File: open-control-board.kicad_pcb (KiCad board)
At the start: 4 copper layers, 69 x 54 mm, 123 parts, among them CN1 Service boiler fill sensor, CN10 LCC Port, CN2 Water tank level switch, CN3 NTC Service Boiler, CN4 NTC Brew Boiler, CN5 Service boiler relay, CN6 Conn_02x04_Counter_Clockwise, CN7 Brew Switch, CN8 12V Separate Supply, CN9 Brew boiler relay, J1 USB_B_Micro, J10 Conn_01x04_Pin, J11 Conn_01x04_Pin, J12 Conn_02x06_Odd_Even, J13 Conn_02x05_Odd_Even, J14 Conn_02x04_Odd_Even, J15 Conn_02x05_Odd_Even, J16 USB_B_Micro, J17 BM04B-SRSS-TB(LF)(SN), J18 Conn_01x03_Pin, J2 BM04B-SRSS-TB(LF)(SN), Q1 AO3401A, Q11 DMN63D8LDW, Q2 AO3401A, Q3 Q_PMOS-E_DUAL_Generic_SEP_S1G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, Q4 DMN63D8LDW, Q5 Q_PMOS-E_DUAL_Generic_SEP_S1G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, Q6 DMN63D8LDW, SW1 SW_Push, SW2 SW_Push, SW3 SW_Push, SW4 SW_Push, U1 TPS82130, U10 FDC1004, U15 STPIC6C595TTR, U16 STPIC6C595TTR, U3 TPS82130, U4 RP2040, U5 ESP32-S3-WROOM-1, U7 TXB0108PWR, U8 ADS1115IDGS, U9 W25Q16JVUXIQ, Y1 XYDBPCNANF-12MHZ

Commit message: Added OSHW logo
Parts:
- added REF**: OSHW-Logo2_9.8x8mm_SilkScreen, Symbol:OSHW-Logo2_9.8x8mm_SilkScreen, B.Cu at (108.0, 59.6)
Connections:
- Q4 pad 3: unconnected-(Q4B-D2-Pad3) -> (no net)
- Q4 pad 4: unconnected-(Q4B-S2-Pad4) -> (no net)
- Q4 pad 5: unconnected-(Q4B-G2-Pad5) -> (no net)

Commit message: R0B changes (WIP)
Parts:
- removed CN1: Service boiler fill sensor, Connector_PinHeader_2.54mm:PinHeader_1x02_P2.54mm_Vertical
- removed D3: KT-0603W, LED_SMD:LED_0603_1608Metric
- removed J10, J11: Conn_01x04_Pin, Connector_PinSocket_2.54mm:PinSocket_1x04_P2.54mm_Vertical
- removed J14: Conn_02x04_Odd_Even, Connector_PinHeader_2.54mm:PinHeader_2x04_P2.54mm_Vertical
- removed J18: Conn_01x03_Pin, Connector_PinHeader_2.54mm:PinHeader_1x03_P2.54mm_Vertical_SMD_Pin1Left
- removed R35: 120R, Resistor_SMD:R_0402_1005Metric
- removed R49, R50: 10K, Resistor_SMD:R_0402_1005Metric
- added C26: C_Small, Capacitor_SMD:C_0402_1005Metric_Pad0.74x0.62mm_HandSolder, F.Cu at (103.4, 33.4)
- added C35: C_Small, Capacitor_SMD:C_0402_1005Metric_Pad0.74x0.62mm_HandSolder, F.Cu at (104.5, 34.5)
- added C36: C_Small, Capacitor_SMD:C_0402_1005Metric_Pad0.74x0.62mm_HandSolder, F.Cu at (108.8, 34.8)
- added C38: C_Small, Capacitor_SMD:C_0402_1005Metric_Pad0.74x0.62mm_HandSolder, F.Cu at (109.8, 33.5)
- added C39: C_Small, Capacitor_SMD:C_0402_1005Metric_Pad0.74x0.62mm_HandSolder, F.Cu at (112.8, 35.8)
- added C40: C_Small, Capacitor_SMD:C_0402_1005Metric_Pad0.74x0.62mm_HandSolder, F.Cu at (112.8, 37.0)
- added C41: C_Small, Capacitor_SMD:C_0402_1005Metric_Pad0.74x0.62mm_HandSolder, F.Cu at (112.8, 42.4)
- added C42: C_Small, Capacitor_SMD:C_0402_1005Metric_Pad0.74x0.62mm_HandSolder, F.Cu at (112.8, 43.6)
- added C43: C_Small, Capacitor_SMD:C_0805_2012Metric_Pad1.18x1.45mm_HandSolder, F.Cu at (110.6, 36.8)
- added C44: C_Small, Capacitor_SMD:C_0805_2012Metric_Pad1.18x1.45mm_HandSolder, F.Cu at (110.6, 43.0)
- added D2: KT-0603W, LED_SMD:LED_0603_1608Metric, F.Cu at (71.9, 46.0)
- added J3: Conn_02x03_Odd_Even, Connector_PinHeader_1.27mm:PinHeader_2x03_P1.27mm_Vertical_SMD, B.Cu at (76.3, 58.1)
- added J4: Conn_01x06_Pin, Connector_PinHeader_2.54mm:PinHeader_1x06_P2.54mm_Vertical, F.Cu at (119.2, 32.9)
- added J5: Conn_02x05_Counter_Clockwise, Connector_PinHeader_2.54mm:PinHeader_2x05_P2.54mm_Vertical, F.Cu at (76.9, 29.9)
- added J6: Conn_01x05_Pin, Connector_PinHeader_2.54mm:PinHeader_1x05_P2.54mm_Vertical, F.Cu at (54.4, 41.8)
- added JP1: SolderJumper_3_Bridged12, Jumper:SolderJumper-3_P1.3mm_Bridged2Bar12_RoundedPad1.0x1.5mm_NumberLabels, B.Cu at (110.7, 52.9)
- added JP10: SolderJumper_3_Bridged12, Jumper:SolderJumper-3_P1.3mm_Bridged2Bar12_RoundedPad1.0x1.5mm_NumberLabels, B.Cu at (110.7, 55.6)
- added JP11: SolderJumper_3_Bridged12, Jumper:SolderJumper-3_P1.3mm_Bridged2Bar12_RoundedPad1.0x1.5mm_NumberLabels, B.Cu at (110.7, 58.2)
- added JP12: SolderJumper_3_Bridged12, Jumper:SolderJumper-3_P1.3mm_Bridged2Bar12_RoundedPad1.0x1.5mm_NumberLabels, B.Cu at (110.7, 60.9)
- added JP14: SolderJumper_2_Open, Jumper:SolderJumper-2_P1.3mm_Open_RoundedPad1.0x1.5mm, B.Cu at (111.2, 41.1)
- added JP15: SolderJumper_2_Open, Jumper:SolderJumper-2_P1.3mm_Open_RoundedPad1.0x1.5mm, B.Cu at (111.2, 46.2)
- added JP16: SolderJumper_3_Bridged12, Jumper:SolderJumper-3_P1.3mm_Bridged2Bar12_RoundedPad1.0x1.5mm_NumberLabels, B.Cu at (60.5, 53.5)
- added JP17: SolderJumper_2_Bridged, Jumper:SolderJumper-2_P1.3mm_Bridged2Bar_RoundedPad1.0x1.5mm, F.Cu at (115.2, 30.9)
- added JP18: SolderJumper_2_Bridged, Jumper:SolderJumper-2_P1.3mm_Bridged2Bar_RoundedPad1.0x1.5mm, F.Cu at (105.7, 30.8)
- added Q7: DMN63D8LDW, PCM_Package_TO_SOT_SMD_AKL:SOT-363_SC-70-6, F.Cu at (93.2, 46.8)
- added R14: R_Small, Resistor_SMD:R_0805_2012Metric_Pad1.20x1.40mm_HandSolder, F.Cu at (98.8, 33.2)
- added R15: R_Small, Resistor_SMD:R_0805_2012Metric_Pad1.20x1.40mm_HandSolder, F.Cu at (106.5, 37.0)
- added R16: R_Small, Resistor_SMD:R_0402_1005Metric_Pad0.72x0.64mm_HandSolder, F.Cu at (107.6, 33.5)
- added R25: R_Small, Resistor_SMD:R_0402_1005Metric_Pad0.72x0.64mm_HandSolder, F.Cu at (115.2, 37.0)
- added R3: 10K, Resistor_SMD:R_0402_1005Metric, F.Cu at (106.0, 57.6)
- added R4: R_Small, Resistor_SMD:R_0402_1005Metric_Pad0.72x0.64mm_HandSolder, F.Cu at (102.2, 33.4)
- added R40: R_Small, Resistor_SMD:R_0805_2012Metric_Pad1.20x1.40mm_HandSolder, F.Cu at (115.2, 34.2)
- added R41: R_Small, Resistor_SMD:R_0805_2012Metric_Pad1.20x1.40mm_HandSolder, F.Cu at (115.2, 38.6)
- added R42: R_Small, Resistor_SMD:R_0805_2012Metric_Pad1.20x1.40mm_HandSolder, F.Cu at (115.2, 40.8)
- added R43: R_Small, Resistor_SMD:R_0805_2012Metric_Pad1.20x1.40mm_HandSolder, F.Cu at (115.2, 45.2)
- added RN3: 10K, PCM_Resistor_SMD_AKL:R_Array_Concave_4x0402, F.Cu at (107.6, 46.2)
- added U11: ADS1115IDGS, Package_SO:TSSOP-10_3x3mm_P0.5mm, F.Cu at (102.6, 41.5)
- added U12: ADS1115IDGS, Package_SO:TSSOP-10_3x3mm_P0.5mm, F.Cu at (102.6, 45.4)
- CN2: value Water tank level switch -> ~
- CN5: value Service boiler relay -> ~
- CN7: value Brew Switch -> ~
- CN9: value Brew boiler relay -> ~
- J1, J16: footprint U-D-M5DS-W-3:U-D-M5DS-W-3 -> Connector_USB:USB_Micro-B_Molex-105133-0001
- JP3, JP7: footprint Connector_PinHeader_2.54mm:PinHeader_1x02_P2.54mm_Vertical -> Connector_PinHeader_1.27mm:PinHeader_1x02_P1.27mm_Vertical
- R19: value R_Small -> 10K; footprint Resistor_THT:R_Axial_DIN0204_L3.6mm_D1.6mm_P5.08mm_Horizontal -> Resistor_SMD:R_0402_1005Metric
- R24, R26, R27: footprint Resistor_THT:R_Axial_DIN0204_L3.6mm_D1.6mm_P5.08mm_Horizontal -> Resistor_SMD:R_0402_1005Metric_Pad0.72x0.64mm_HandSolder
- R31: value 10K -> 120R
- U8: value ADS1115IDGS -> TXB0108PWR; footprint Package_SO:TSSOP-10_3x3mm_P0.5mm -> Package_SO:TSSOP-20_4.4x6.5mm_P0.65mm
- moved Q5 54.8 mm to (59.2, 43.4), turned to 180 degrees
- moved Q3 54.7 mm to (59.3, 47.6), turned to 180 degrees
- moved JP6 49.6 mm to (60.5, 50.1)
- moved JP4 49.6 mm to (60.4, 42.5)
- moved JP5 49.6 mm to (60.4, 46.2)
- moved R30 49.3 mm to (62.1, 46.6), turned to 90 degrees
- moved R29 49.2 mm to (62.1, 44.5), turned to 90 degrees
- moved R28 49.1 mm to (62.1, 42.4), turned to 90 degrees
- moved R19 48.6 mm to (62.1, 48.6), turned to 90 degrees
- moved J17 35.7 mm to (65.5, 53.5)
- moved R36 35.7 mm to (64.0, 55.3)
- moved R37 35.7 mm to (66.0, 55.3)
- moved J15 28.6 mm to (87.4, 58.0)
- moved R20 27.0 mm to (97.3, 58.9), turned to 0 degrees
- moved R21 26.3 mm to (97.3, 57.8), turned to 0 degrees
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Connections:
- net GP15 renamed RP2040_SERIAL_BOOT
- C2 pad 2: +12V -> VIN
- CN2 pad 1: WATER_TANK_LVL_SW -> VIN
- CN2 pad 2: GND -> CN9_DRAIN
- CN3 pad 1: AVCC -> ADC1_AIN2_COND
- CN3 pad 2: SERVICE_BOILER_NTC -> ADC1_AIN3
- CN4 pad 1: AVCC -> ADC1_AIN0_COND
- CN4 pad 2: BREW_BOILER_NTC -> ADC1_AIN1
- CN5 pad 1: CN5_DRAIN -> VIN
- CN5 pad 2: +12V -> CN5_DRAIN
- CN6 pad 2: +12V -> VIN
- CN7 pad 1: BREW_SW -> WATER_TANK_LVL_SW
- CN8 pad 1: +12V -> VIN
- CN9 pad 1: +12V -> BREW_SW
- CN9 pad 2: CN9_DRAIN -> GND
- J12 pad 2: +3V3 -> +5V
- JP2 pad 1: +12V -> VIN
- JP3 pad 2: +5V -> VIN
- JP4 pad 1: +12V -> VIN
- JP5 pad 1: +12V -> VIN
- JP6 pad 1: +12V -> VIN
- JP7 pad 2: +5V -> VIN
- Q2 pad 2: +12V -> VIN
- Q3 pad 1: VOUT_2_GATE -> VOUT_4_GATE
- Q3 pad 5: Net-(JP5-C) -> Net-(JP16-C)
- Q3 pad 6: VOUT_2 -> VOUT_4
- Q4 pad 1: ADS1115_RDY -> INT_SCL
- Q4 pad 3: (no net) -> INT_SDA_AVCC
- Q4 pad 4: (no net) -> INT_SDA
- Q4 pad 5: (no net) -> +3V3
- Q4 pad 6: ADS1115_RDY_AVCC -> INT_SCL_AVCC
- Q5 pad 1: (no net) -> VOUT_2_GATE
- Q5 pad 5: (no net) -> Net-(JP5-C)
- Q5 pad 6: (no net) -> VOUT_2
- Q6 pad 1: INT_SDA -> ADS1115_1_RDY
- Q6 pad 3: INT_SCL_AVCC -> ADS1115_2_RDY_AVCC
- Q6 pad 4: INT_SCL -> ADS1115_2_RDY
- Q6 pad 6: INT_SDA_AVCC -> ADS1115_1_RDY_AVCC
- R19 pad 1: AGND -> Net-(JP16-C)
- R19 pad 2: AIN1 -> VOUT_4_GATE
- R2 pad 2: +12V -> VIN
- R20 pad 1: INT_SDA -> INT_SCL
- R21 pad 1: INT_SCL -> INT_SDA
- R24 pad 1: AGND -> ADC2_AIN0_COND
- R24 pad 2: AIN0 -> ADC2_AIN0
- R26 pad 1: SERVICE_BOILER_NTC -> ADC2_AIN2_COND
- R26 pad 2: AGND -> ADC2_AIN2
- R27 pad 1: AGND -> ADC2_AIN3_COND
- R27 pad 2: BREW_BOILER_NTC -> ADC2_AIN3
- R31 pad 1: SR_OE -> Net-(U5-GPIO8/TOUCH8/ADC1_CH7/SUBSPICS1)
- R31 pad 2: GND -> Net-(D2-A)
- RN2 pad 1: INT_SDA_AVCC -> INT_SCL
- RN2 pad 2: INT_SCL_AVCC -> INT_SDA
- RN2 pad 3: INT_SDA -> INT_SDA_AVCC
- RN2 pad 4: INT_SCL -> INT_SCL_AVCC
- RN2 pad 5: +3V3 -> AVCC
- RN2 pad 6: +3V3 -> AVCC
- RN2 pad 7: AVCC -> +3V3
- RN2 pad 8: AVCC -> +3V3
- U1 pad 1: +12V -> VIN
- U1 pad 2: +12V -> VIN
- U16 pad 12: unconnected-(U16-DRAIN5-Pad12) -> VOUT_4_GATE
- U4 pad 11: INT_SCL -> INT_SDA
- U4 pad 12: INT_SDA -> INT_SCL
- U4 pad 13: ESP32_RP2040_UART1 -> SRCK_3V3
- U4 pad 14: ESP32_RP2040_UART2 -> unconnected-(U4-GPIO11-Pad14)
- U4 pad 29: GP18 -> GP18_3V3
- U4 pad 30: GP19 -> GP19_3V3
- U4 pad 31: GP20 -> GP20_3V3
- U4 pad 32: GP21 -> GP21_3V3
- U4 pad 6: SRCK_3V3 -> ESP32_RP2040_UART1
- U4 pad 7: ADS1115_RDY -> ESP32_RP2040_UART2
- U4 pad 8: QWIIC_SCL -> QWIIC_SDA
- U4 pad 9: QWIIC_SDA -> QWIIC_SCL
- U5 pad 11: ESP32_RP2040_UART1 -> unconnected-(U5-GPIO18/U1RXD/ADC2_CH7/CLK_OUT3-Pad11)
- U5 pad 12: GP26 -> Net-(U5-GPIO8/TOUCH8/ADC1_CH7/SUBSPICS1)
- U5 pad 17: GP27 -> unconnected-(U5-GPIO9/TOUCH9/ADC1_CH8/FSPIHD/SUBSPIHD-Pad17)
- U5 pad 18: GP28 -> ESP32_QWIIC_SDA
- U5 pad 19: GP29 -> ESP32_QWIIC_SCL
- U5 pad 23: ESP32_RP2040_UART2 -> unconnected-(U5-GPIO21-Pad23)
- U5 pad 25: Net-(U5-GPIO48/SPICLK_N/SUBSPICLK_N_DIFF) -> unconnected-(U5-GPIO48/SPICLK_N/SUBSPICLK_N_DIFF-Pad25)
- U5 pad 36: Net-(J18-Pin_1) -> ESP32_U0RXD
- U5 pad 37: Net-(J18-Pin_2) -> ESP32_U0TXD
- U5 pad 38: ESP32_QWIIC_SDA -> ESP32_RP2040_UART2
- U5 pad 39: ESP32_QWIIC_SCL -> ESP32_RP2040_UART1
- U5 pad 4: GP18 -> GP18_3V3
- U5 pad 5: GP19 -> GP19_3V3
- U5 pad 6: GP20 -> GP20_3V3
- U5 pad 7: GP21 -> GP21_3V3
- U5 pad 8: unconnected-(U5-GPIO15/U0RTS/ADC2_CH4/XTAL_32K_P-Pad8) -> ESP32_BOOTSEL_RP2040
- U5 pad 9: unconnected-(U5-GPIO16/U0CTS/ADC2_CH5/XTAL_32K_N-Pad9) -> ESP32_DISABLE_RP2040
- U7 pad 1: CN6_2_3V3 -> CN6_4_3V3
- U7 pad 10: SER_IN_3V3 -> SR_OE
- U7 pad 11: SER_IN_5V -> GND
- U7 pad 12: SRCLR_5V -> SER_IN_5V
- U7 pad 13: nG_5V -> SRCLR_5V
- U7 pad 14: RCLK_5V -> nG_5V
- U7 pad 15: GND -> RCLK_5V
- U7 pad 16: +5V -> SRCK_5V
- U7 pad 17: SRCK_5V -> CN6_2_5V
- U7 pad 18: CN6_2_5V -> CN6_3_5V
- U7 pad 19: CN6_3_5V -> +5V
- U7 pad 2: CN6_3_3V3 -> +3V3
- U7 pad 3: CN6_4_3V3 -> CN6_3_3V3
- U7 pad 4: SRCK_3V3 -> CN6_2_3V3
- U7 pad 5: +3V3 -> SRCK_3V3
- U7 pad 6: SR_OE -> RCLK_3V3
- U7 pad 7: RCLK_3V3 -> nG_3V3
- U7 pad 8: nG_3V3 -> SRCLR_3V3
- U7 pad 9: SRCLR_3V3 -> SER_IN_3V3
- U8 pad 1: AGND -> GP21_3V3
- U8 pad 10: INT_SCL_AVCC -> SR_OE
- U8 pad 2: ADS1115_RDY_AVCC -> +3V3
- U8 pad 3: AGND -> GP20_3V3
- U8 pad 4: AIN0 -> GP19_3V3
- U8 pad 5: AIN1 -> GP18_3V3
- U8 pad 6: BREW_BOILER_NTC -> unconnected-(U8-A5-Pad6)
- U8 pad 7: SERVICE_BOILER_NTC -> unconnected-(U8-A6-Pad7)
- U8 pad 8: AVCC -> unconnected-(U8-A7-Pad8)
- U8 pad 9: INT_SDA_AVCC -> unconnected-(U8-A8-Pad9)
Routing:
- net +12V: track 233.6 -> 0.00 mm, vias 2 -> 0
- net VIN: track 0.00 -> 210.2 mm, vias 0 -> 2
- net GP21_3V3: track 0.00 -> 73.4 mm, vias 0 -> 3
- net GP19_3V3: track 0.00 -> 72.2 mm, vias 0 -> 3
- net GP18_3V3: track 0.00 -> 68.8 mm, vias 0 -> 3
- net GP20_3V3: track 0.00 -> 68.1 mm, vias 0 -> 3
- net ESP32_TMS: track 71.6 -> 13.7 mm, vias 1 -> 2
- net ESP32_TDO: track 63.7 -> 11.4 mm, vias 1 -> 2
- net ESP32_TDI: track 62.1 -> 9.99 mm, vias 1 -> 2
- net ESP32_TCK: track 65.1 -> 13.2 mm, vias 1 -> 2
- net +3V3: track 359.0 -> 311.8 mm, vias 18 -> 24
- net VOUT_4_GATE: track 0.00 -> 42.0 mm, vias 0 -> 2
- net GP19: track 50.8 -> 9.56 mm, vias 2 -> 0
- net GP20: track 50.5 -> 9.53 mm, vias 3 -> 0
- net Net-(J18-Pin_1): track 39.8 -> 0.00 mm, vias 2 -> 0
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- added copper zone on F.Cu, net VIN
- removed copper zone on F.Cu, net +12V
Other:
- board text added: "CN10 UART TX Verified"
- board text added: "J12 Verified"
- board text removed: "ESP32 EN"
- board text removed: "ESP32 GPIO0"
- board text removed: "RP2040 Boot"
- board text removed: "RP2040 Reset"

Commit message: WIP
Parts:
- removed C35, C36: C_Small, Capacitor_SMD:C_0402_1005Metric_Pad0.74x0.62mm_HandSolder
- C26, C38, C39, C40, C41, C42, C43, C44: value C_Small -> 100 nF
- R16, R24, R25, R26, R27, R4: value R_Small -> 1K
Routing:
- net AGND: track 20.8 -> 14.2 mm, vias 6 -> 7
- net ADC1_AIN0: track 11.2 -> 10.2 mm
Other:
- board text added: "Rev R0B"
- board text removed: "Rev R0A"

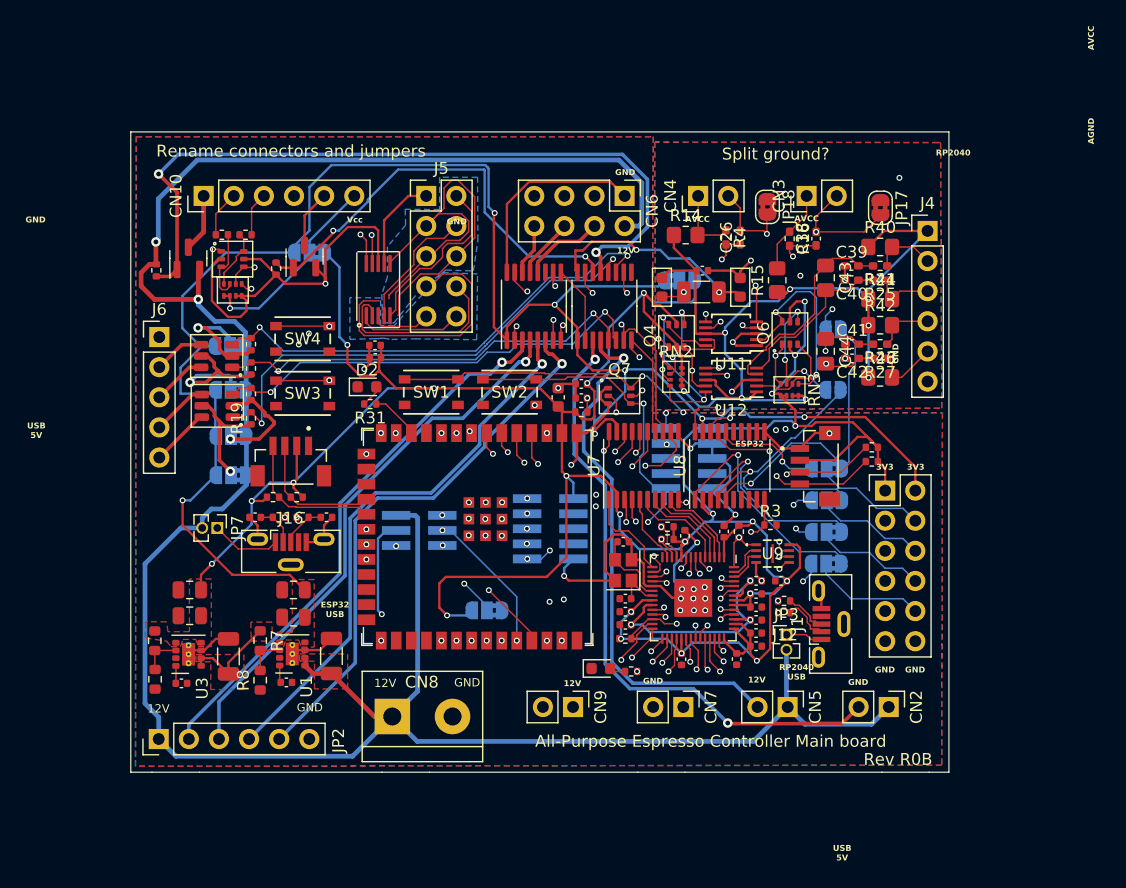
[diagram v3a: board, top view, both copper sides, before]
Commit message: Renamed connectors and added a lot of silk screen
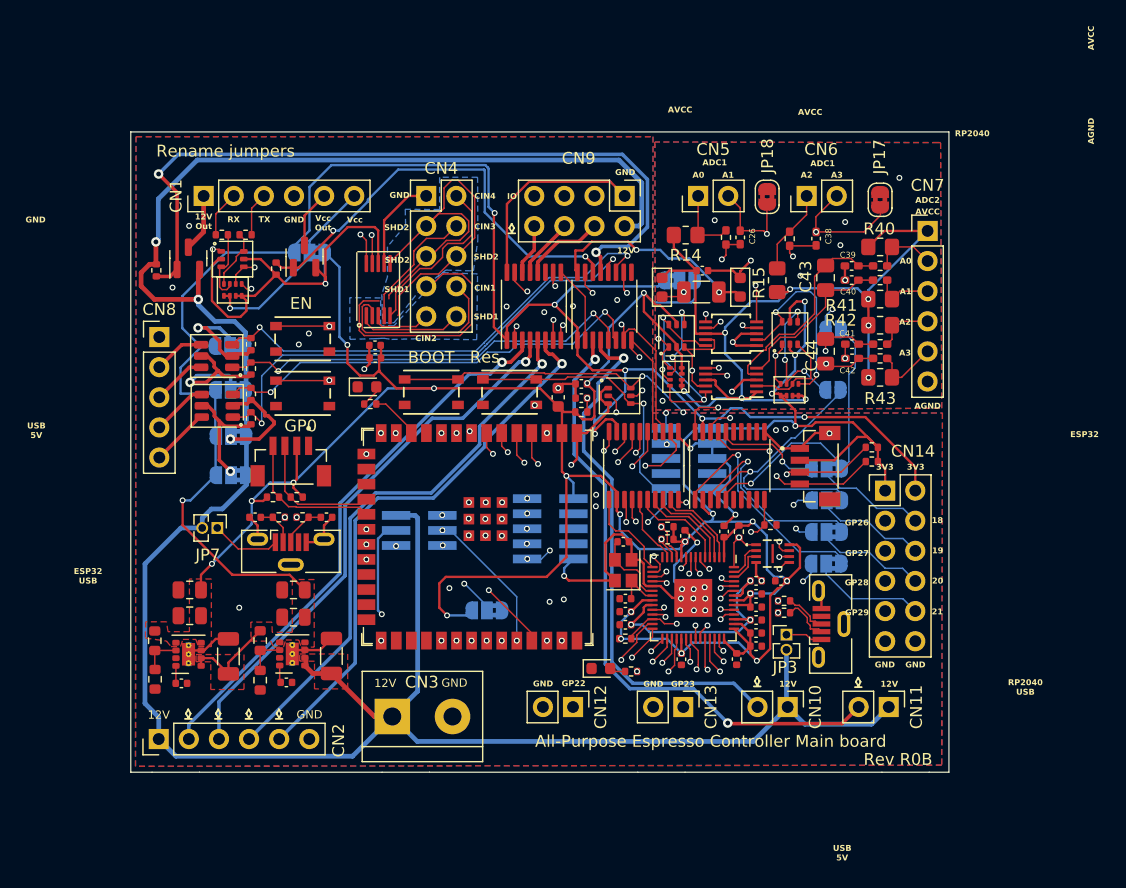
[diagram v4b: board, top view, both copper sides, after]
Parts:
- U7, U8: value TXB0108PWR -> TXS0108EPWR
- moved REF** 69.5 mm to (60.5, 67.8)
- moved JP18 0.85 mm to (105.7, 30.0)
- moved JP17 0.68 mm to (115.2, 30.2)
- renumbered CN10 to CN1, CN5 to CN10, CN2 to CN11, CN9 to CN12, CN7 to CN13, J12 to CN14, JP2 to CN2, CN8 to CN3, J5 to CN4, CN4 to CN5, CN3 to CN6, J4 to CN7, J6 to CN8, CN6 to CN9
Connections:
- net CN10_12V_GATE renamed CN1_12V_GATE
- net CN10_3V3_GATE renamed CN1_3V3_GATE
- net CN10_UART_RX renamed CN1_UART_RX
- net CN10_UART_RX_SHIFT_SEL renamed CN1_UART_RX_SHIFT_SEL
- net CN10_UART_TX renamed CN1_UART_TX
- net CN10_UART_TX_SHIFT_SEL renamed CN1_UART_TX_SHIFT_SEL
- net CN10_UART_VCC renamed CN1_UART_VCC
- net CN5_DRAIN renamed CN10_DRAIN
- net CN6_2_3V3 renamed CN9_2_3V3
- net CN6_2_5V renamed CN9_2_5V
- net CN6_3_3V3 renamed CN9_3_3V3
- net CN6_3_5V renamed CN9_3_5V
- net CN6_4 renamed CN9_4
- net CN6_4_3V3 renamed CN9_4_3V3
- net CN6_4_5V renamed CN9_4_5V
- net CN6_6 renamed CN9_6
- net CN6_8 renamed CN9_8
- net CN9_DRAIN renamed CN11_DRAIN
- net JP2_FA10 renamed CN2_FA10
- net JP2_FA7 renamed CN2_FA7
- net JP2_FA8 renamed CN2_FA8
- net JP2_FA9 renamed CN2_FA9
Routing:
- net ADC1_AIN1: track 14.9 -> 16.0 mm
- net ADC1_AIN3: track 23.0 -> 23.7 mm
- net GND: vias 31 -> 39
- net AGND: vias 7 -> 11
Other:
- board text added: "1"
- board text added: "12V Out"
- board text added: "18"
- board text added: "19"
- board text added: "2"
- board text added: "20"
- board text added: "21"
- board text added: "3"
- board text added: "4"
- board text added: "A0"
- board text added: "A1"
- board text added: "A2"
- board text added: "A3"
- board text added: "ADC1"
- board text added: "ADC1 RDY -> GP18"
- board text added: "ADC2"
- board text added: "ADC2 RDY -> GP19"
- board text added: "BOOT"
- board text added: "CIN1"
- board text added: "CIN2"
- board text added: "CIN3"
- board text added: "CIN4"
- board text added: "EN"
- board text added: "ESP-Prog JTAG"
- board text added: "ESP-Prog UART"
- board text added: "GP0"
- board text added: "GP18"
- board text added: "GP18-21 V"
- board text added: "GP19"
- board text added: "GP20"
- board text added: "GP21"
- board text added: "GP22"
- board text added: "GP23"
- board text added: "GP26"
- board text added: "GP27"
- board text added: "GP28"
- board text added: "GP29"
- board text added: "IO"
- board text added: "RESET"
- board text added: "RP2040 SWD"
- board text added: "Rename jumpers"
- board text added: "Res"
- board text added: "SHD1"
- board text added: "SHD2"
- board text added: "SWCLK"
- board text added: "SWD"
- board text added: "TCK"
- board text added: "TDI"
- board text added: "TDO"
- board text added: "TMS"
- board text added: "VIN"
- board text added: "VOUT V"
- board text added: "Vcc Out"
- board text removed: "RP2040 DBG"
- board text removed: "Rename connectors and jumpers"
- board text removed: "Split ground?"
- board text removed: "UART"
- board text removed: "VOUT1 V"
- board text removed: "VOUT2 V"
- board text removed: "VOUT3 V"

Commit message: Updated PCB with screw holes
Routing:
- net VIN: track 210.2 -> 209.1 mm
- net GND: vias 39 -> 41
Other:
- outline, holes or cut-outs redrawn
- board text removed: "ESP32"
- board text removed: "ESP32 JTAG"
- board text removed: "ESP32 USB"
- board text removed: "J12 Verified"
- board text removed: "RP2040"
- board text removed: "RP2040 USB"
- board text removed: "USB 5V"

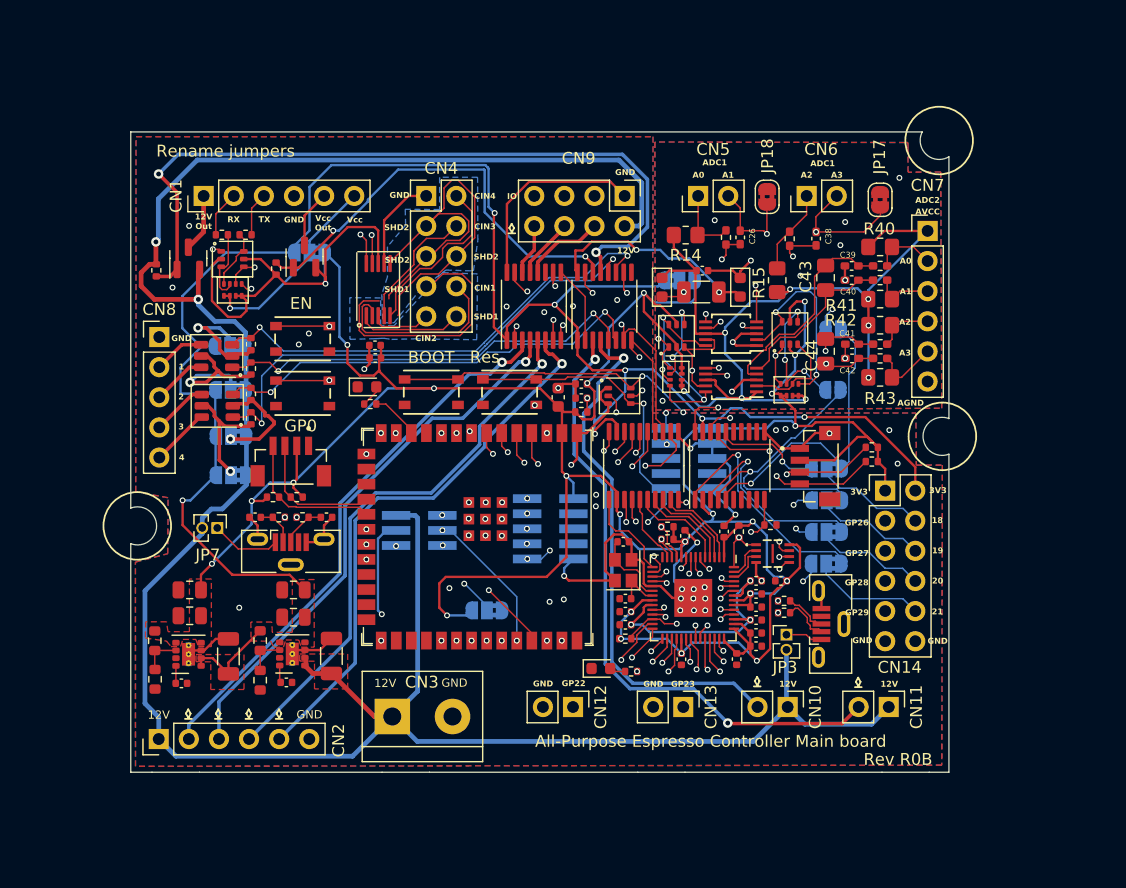
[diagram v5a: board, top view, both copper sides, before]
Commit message: Changed mounting holes to M2 (to match HV board) and use actual footprints
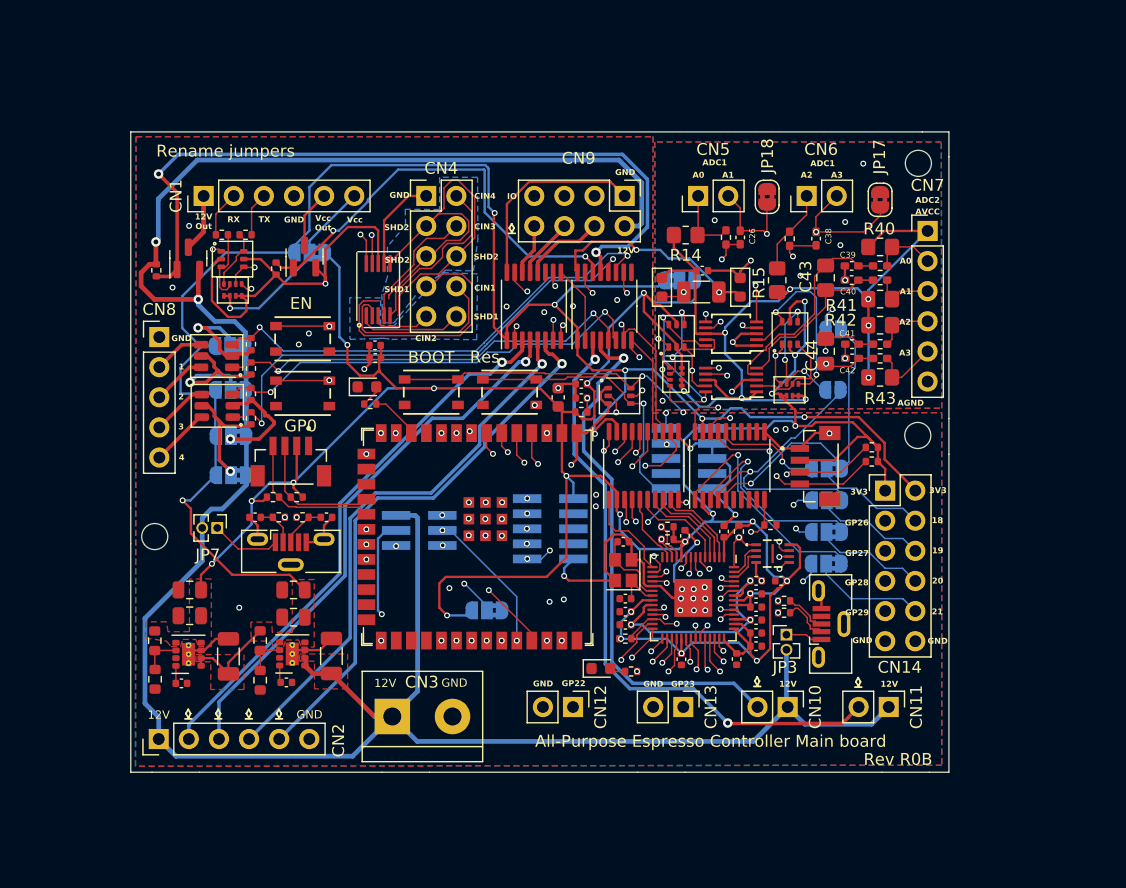
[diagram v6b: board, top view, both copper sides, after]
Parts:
- added H1: MountingHole, MountingHole:MountingHole_2.2mm_M2, F.Cu at (118.4, 27.1)
- added H2: MountingHole, MountingHole:MountingHole_2.2mm_M2, F.Cu at (118.4, 50.1)
- added H3: MountingHole, MountingHole:MountingHole_2.2mm_M2, F.Cu at (54.0, 58.6)
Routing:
- net GND: vias 41 -> 39
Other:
- outline, holes or cut-outs redrawn
- board text removed: "Connector height: 10.16 mm over board"
